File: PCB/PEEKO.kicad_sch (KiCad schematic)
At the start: 26 parts, among them J1 Rasberry PI Pico, J2 Conn_02x15_Odd_Even, J3 Conn_01x02_Pin, J4 Conn_01x02_Pin, U1 TXU0104, U2 TXU0104, U3 TXU0104, U4 TXU0104, U5 TXU0104, U6 TXU0104

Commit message: boms
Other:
- moved on the sheet: D1, R1
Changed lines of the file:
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@@
 	)
 	(junction
-		(at 95.25 158.75)
-		(diameter 0)
-		(color 0 0 0 0)
-	)
-	(junction
 		(at 53.34 57.15)
 		(diameter 0)
@@
 	)
 	(junction
+		(at 88.9 158.75)
+		(diameter 0)
+		(color 0 0 0 0)
+	)
+	(junction
 		(at 266.7 101.6)
 		(diameter 0)
@@
 	(wire
 		(pts
-			(xy 95.25 158.75) (xy 95.25 161.29)
+			(xy 223.52 71.12) (xy 223.52 73.66)
 		)
 		(stroke
@@
 	(wire
 		(pts
-			(xy 223.52 71.12) (xy 223.52 73.66)
+			(xy 22.86 41.91) (xy 22.86 44.45)
 		)
 		(stroke
@@
 	(wire
 		(pts
-			(xy 22.86 41.91) (xy 22.86 44.45)
+			(xy 22.86 76.2) (xy 26.67 76.2)
 		)
 		(stroke
@@
 	(wire
 		(pts
-			(xy 22.86 76.2) (xy 26.67 76.2)
+			(xy 22.86 69.85) (xy 22.86 76.2)
 		)
 		(stroke
@@
 	(wire
 		(pts
-			(xy 22.86 69.85) (xy 22.86 76.2)
+			(xy 88.9 158.75) (xy 97.79 158.75)
 		)
 		(stroke
@@
 	(wire
 		(pts
+			(xy 88.9 158.75) (xy 88.9 161.29)
+		)
+		(stroke
+			(width 0)
+			(type default)
+		)
+	)
+	(wire
+		(pts
 			(xy 215.9 121.92) (xy 215.9 114.3)
 		)
@@
 	(wire
 		(pts
-			(xy 102.87 158.75) (xy 133.35 158.75)
+			(xy 105.41 158.75) (xy 133.35 158.75)
 		)
 		(stroke
@@
 	(wire
 		(pts
-			(xy 31.75 158.75) (xy 95.25 158.75)
+			(xy 31.75 158.75) (xy 88.9 158.75)
 		)
 		(stroke
@@
 	)
 	(label "TRIGGER"
-		(at 95.25 158.75 180)
+		(at 97.79 158.75 180)
 		(fields_autoplaced yes)
 		(effects
@@
 	)
 	(label "CHAIN"
-		(at 102.87 158.75 0)
+		(at 105.41 158.75 0)
 		(fields_autoplaced yes)
 		(effects
@@
 	(symbol
 		(lib_id "power:GND")
-		(at 95.25 168.91 0)
+		(at 88.9 168.91 0)
 		(unit 1)
 		(exclude_from_sim no)
@@
 		(fields_autoplaced yes)
 		(property "Reference" "#PWR01"
-			(at 95.25 175.26 0)
+			(at 88.9 175.26 0)
 			(effects
 				(font
@@
 		)
 		(property "Value" "GND"
-			(at 95.25 173.99 0)
+			(at 88.9 173.99 0)
 			(effects
 				(font
@@
 		)
 		(property "Footprint" ""
-			(at 95.25 168.91 0)
+			(at 88.9 168.91 0)
 			(effects
 				(font
@@
 		)
 		(property "Datasheet" ""
-			(at 95.25 168.91 0)
+			(at 88.9 168.91 0)
 			(effects
 				(font
@@
 		)
 		(property "Description" "Power symbol creates a global label with name \"GND\" , ground"
-			(at 95.25 168.91 0)
+			(at 88.9 168.91 0)
 			(effects
 				(font
@@
 	(symbol
 		(lib_id "Device:R")
-		(at 95.25 165.1 180)
+		(at 88.9 165.1 180)
 		(unit 1)
 		(exclude_from_sim no)
@@
 		(dnp no)
 		(property "Reference" "R1"
-			(at 99.314 163.322 0)
+			(at 92.964 163.322 0)
 			(effects
 				(font
@@
 		)
 		(property "Value" "100k"
-			(at 99.822 165.608 0)
+			(at 93.472 165.608 0)
 			(effects
 				(font
@@
 		)
 		(property "Footprint" "000_LOCAL:R_0805"
-			(at 97.028 165.1 90)
+			(at 90.678 165.1 90)
 			(effects
 				(font
@@
 		)
 		(property "Datasheet" "datasheets/PYu-RC_Group_51_RoHS_L_12.pdf"
-			(at 95.25 165.1 0)
+			(at 88.9 165.1 0)
 			(effects
 				(font
@@
 		)
 		(property "Description" "RES 100K OHM 1% 1/8W 0805"
-			(at 95.25 165.1 0)
+			(at 88.9 165.1 0)
 			(effects
 				(font
@@
 		)
 		(property "MPN" "RC0805FR-07100KL"
-			(at 95.25 165.1 0)
+			(at 88.9 165.1 0)
 			(effects
 				(font
@@
 	(symbol
 		(lib_id "000_LOCAL:LL4148")
-		(at 99.06 158.75 0)
+		(at 101.6 158.75 0)
 		(unit 1)
 		(exclude_from_sim no)
@@
 		(fields_autoplaced yes)
 		(property "Reference" "D1"
-			(at 99.06 152.4 0)
+			(at 101.6 152.4 0)
 			(effects
 				(font
@@
 		)
 		(property "Value" "LL4148"
-			(at 99.06 154.94 0)
+			(at 101.6 154.94 0)
 			(effects
 				(font
@@
 		)
 		(property "Footprint" "000_LOCAL:D_MiniMELF"
-			(at 99.06 158.75 0)
+			(at 101.6 158.75 0)
 			(effects
 				(font
@@
 		)
 		(property "Datasheet" "datasheets/ll4148.pdf"
-			(at 99.06 158.75 0)
+			(at 101.6 158.75 0)
 			(effects
 				(font
@@
 		)
 		(property "Description" "50V 1A General Purpose Rectifier Diode"
-			(at 99.06 158.75 0)
+			(at 101.6 158.75 0)
 			(effects
 				(font
@@
 		)
 		(property "MPN" "FDLL4148"
-			(at 99.06 158.75 0)
+			(at 101.6 158.75 0)
 			(effects
 				(font

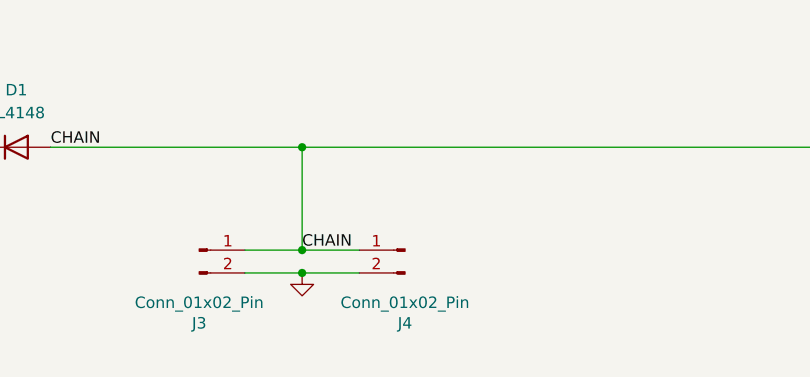
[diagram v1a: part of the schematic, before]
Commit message: shorten chain trace, delete duplicate footprints
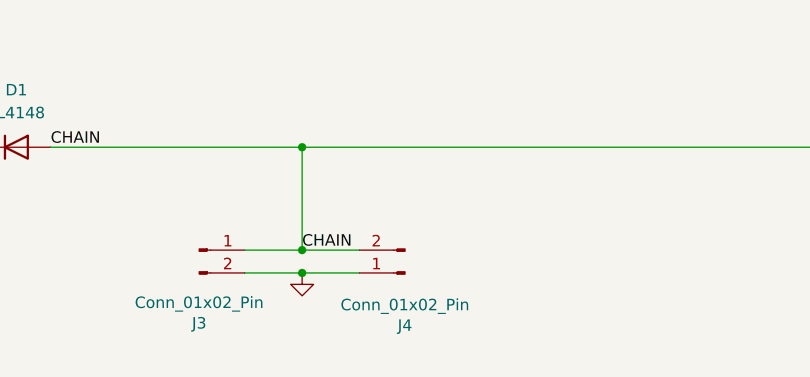
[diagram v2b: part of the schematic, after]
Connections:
- net CHAIN: now also J4.2 (Pin_2); no longer J4.1 (Pin_1)
- net GND: now also J4.1 (Pin_1); no longer J4.2 (Pin_2)
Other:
- moved on the sheet: J4
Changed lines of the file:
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@@
 	(title_block
 		(title "PEEKO")
-		(date "2024-10-05")
-		(rev "003")
+		(date "2025-02-09")
+		(rev "004")
 		(comment 1 "based on github.com/gusmanb/logicanalyzer")
 		(comment 2 "github.com/bkw777/peeko")
@@
 	(symbol
 		(lib_id "000_LOCAL:Conn_01x02_Pin")
-		(at 144.78 170.18 0)
-		(mirror y)
+		(at 144.78 172.72 180)
 		(unit 1)
 		(exclude_from_sim no)
@@
 		(dnp no)
 		(property "Reference" "J4"
-			(at 144.78 178.308 0)
+			(at 144.78 178.562 0)
 			(effects
 				(font
@@
 		)
 		(property "Value" "Conn_01x02_Pin"
-			(at 144.78 176.022 0)
+			(at 144.78 176.276 0)
 			(effects
 				(font
@@
 		)
 		(property "Footprint" "000_LOCAL:PinHeader_1x02_P2.54mm_Horizontal"
-			(at 144.78 170.18 0)
+			(at 144.78 172.72 0)
 			(effects
 				(font
@@
 		)
 		(property "Datasheet" "~"
-			(at 144.78 170.18 0)
+			(at 144.78 172.72 0)
 			(effects
 				(font
@@
 		)
 		(property "Description" "CONN HEADER R/A 2POS 2.54MM"
-			(at 144.78 170.18 0)
+			(at 144.78 172.72 0)
 			(effects
 				(font
@@
 		)
 		(property "MPN" "PH1RB-02-UA"
-			(at 144.78 170.18 0)
+			(at 144.78 172.72 0)
 			(effects
 				(font

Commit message: zigzag pi pico dip pins for friction fit
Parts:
- J1: footprint 000_LOCAL:dip-40-700-pi-pico -> 000_LOCAL:dip-40-700-pi-pico-z
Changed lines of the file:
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@@
 	(title_block
 		(title "PEEKO")
-		(date "2025-02-09")
-		(rev "004")
+		(date "2025-03-31")
+		(rev "005")
 		(comment 1 "based on github.com/gusmanb/logicanalyzer")
 		(comment 2 "github.com/bkw777/peeko")
@@
 			)
 		)
-		(property "Footprint" "000_LOCAL:dip-40-700-pi-pico"
+		(property "Footprint" "000_LOCAL:dip-40-700-pi-pico-z"
 			(at 241.3 95.25 90)
 			(effects
